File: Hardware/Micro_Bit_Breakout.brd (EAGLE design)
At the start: 68.6 x 12.7 mm, 9 parts, among them J1 M22LOCK, X1 EDGE-80PTH-RA

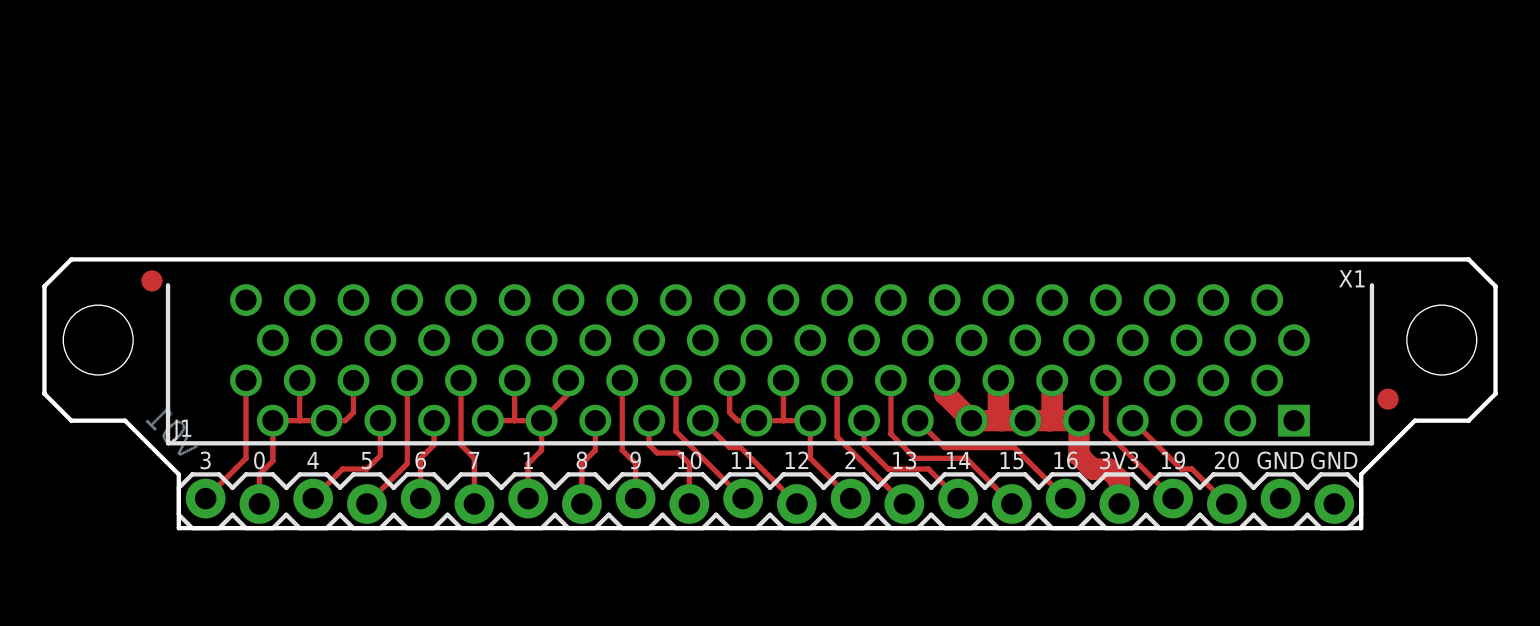
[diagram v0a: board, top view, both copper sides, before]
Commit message: Moved brd outline down
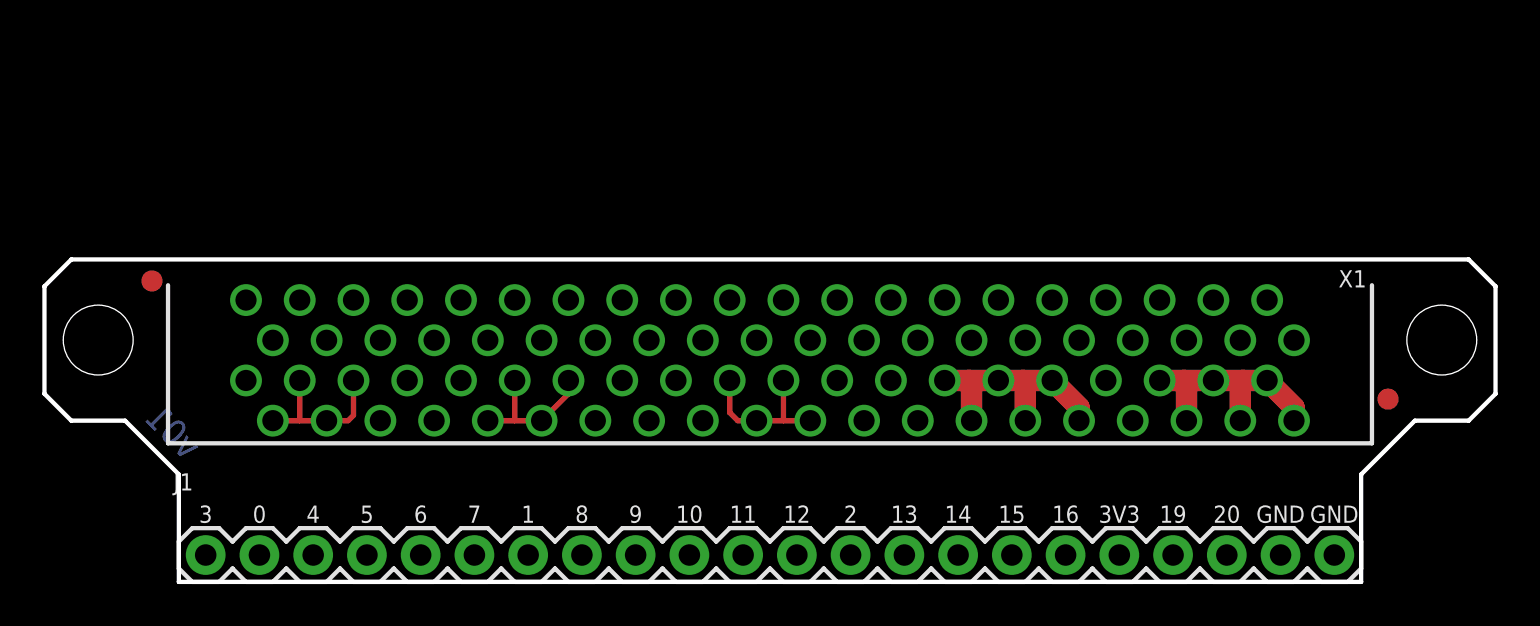
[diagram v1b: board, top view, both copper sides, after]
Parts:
- J1: value M22LOCK -> M22PTH; device SparkFun-Connectors:1X22_LOCK -> local_lib:1X22
- X1: device SparkFun-Connectors:VEC-127-080-R -> local_lib:VEC-127-080-R
- moved J1 2.54 mm to (61.0, -1.27)
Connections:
- net N$10 renamed 12
- net N$11 renamed 11
- net N$12 renamed 10
- net N$13 renamed 9
- net N$14 renamed 8
- net N$15 renamed 1
- net N$17 renamed 7
- net N$18 renamed 6
- net N$19 renamed 5
- net N$2 renamed 16
- net N$20 renamed 4
- net N$21 renamed 0
- net N$22 renamed 3
- net N$3 renamed 20
- net N$4 renamed 19
- net N$5 renamed 3V3
- net N$6 renamed 15
- net N$7 renamed 14
- net N$8 renamed 13
- net N$9 renamed 2
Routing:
- net GND: track 0.00 -> 11.4 mm
- net 15: track 9.62 -> 0.00 mm
- net 16: track 8.51 -> 0.00 mm
- net 13: track 7.15 -> 0.00 mm
- net 19: track 6.90 -> 0.00 mm
- net 11: track 6.90 -> 0.00 mm
- net 14: track 6.64 -> 0.00 mm
- net 5: track 6.63 -> 0.00 mm
- net 3: track 6.37 -> 0.00 mm
- net 7: track 6.10 -> 0.00 mm
- net 12: track 6.08 -> 0.00 mm
- net 20: track 6.08 -> 0.00 mm
- net 9: track 5.85 -> 0.00 mm
- net 4: track 5.67 -> 0.00 mm
- net 10: track 5.32 -> 0.00 mm
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- removed copper zone on layer 1, net GND
- removed copper zone on layer 16, net GND
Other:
- board size 68.6 x 12.7 mm -> 68.6 x 15.2 mm

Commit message: Changed layout to have pin numbers in order. Added prettier silk.
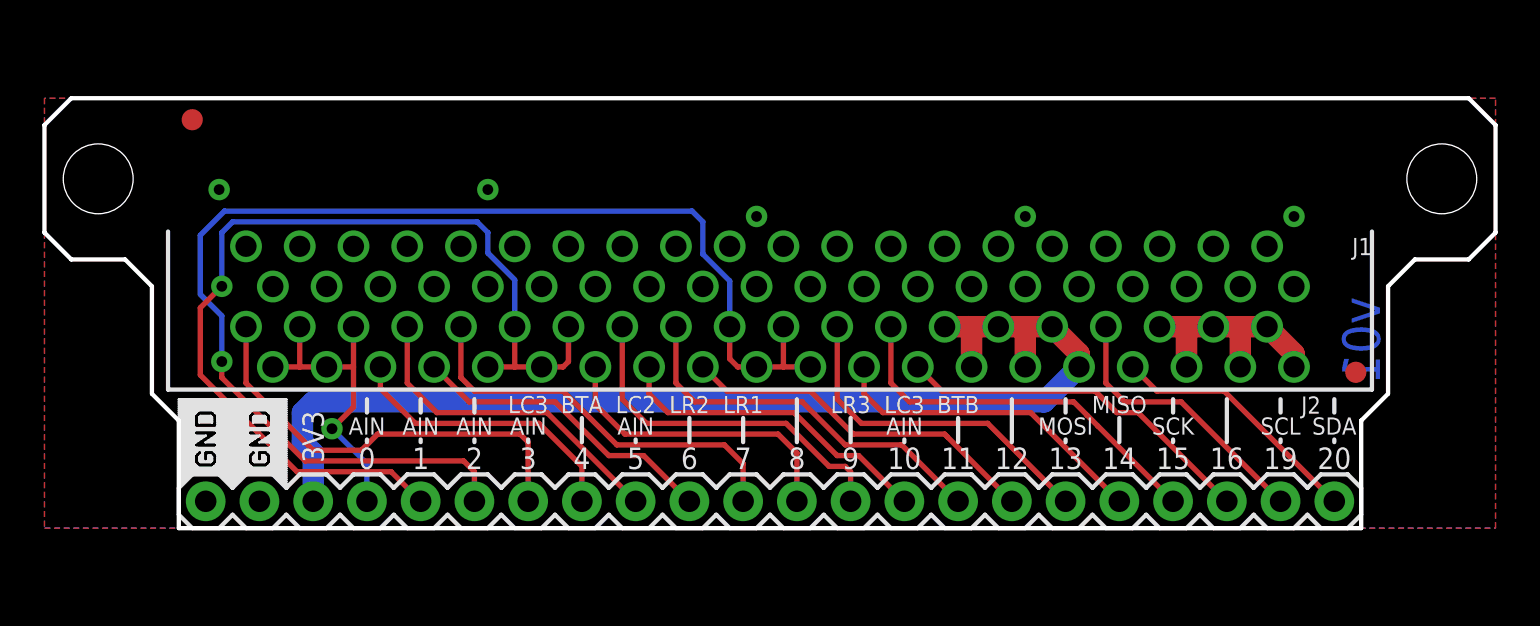
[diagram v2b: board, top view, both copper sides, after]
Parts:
- removed LOGO1: SFE_LOGO_FLAME.1_INCH, SparkFun-Aesthetics:SFE_LOGO_FLAME_.1
- removed X1: EDGE-80PTH-RA, local_lib:VEC-127-080-R
- added J2: M22PTH, local_lib:1X22
- added LOGO2: SFE_LOGO_NAME_FLAME.1_INCH, SparkFun-Aesthetics:SFE_LOGO_NAME_FLAME_.1
- added U$1, U$2: (no value), negasilk:NEGASILK_MICRO_BIT_BREAKOUT
- J1: value M22PTH -> EDGE-80PTH-RA; device local_lib:1X22 -> local_lib:VEC-127-080-R
- moved LOGO3 50.2 mm to (12.4, 17.1)
- moved J1 28.1 mm to (34.3, 7.62)
- moved FRAME1 12.0 mm to (0.00, -11.4)
- moved FD1 7.85 mm to (6.99, 19.3)
- moved H1 7.62 mm to (2.54, 16.5)
- moved H2 7.62 mm to (66.0, 16.5)
- moved FD2 1.98 mm to (62.0, 7.37)
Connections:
- net 0: now also J1.A36, J1.A37, J1.A38, J1.A39, J2.4; no longer J1.21, X1.A36, X1.A37, X1.A38, X1.A39
- net 1: now also J1.A28, J1.A29, J1.A30, J1.A31, J2.5; no longer J1.16, X1.A28, X1.A29, X1.A30, X1.A31
- net 10: now also J1.A25, J2.14; no longer J1.13, X1.A25
- net 11: now also J1.A24, J2.15; no longer J1.12, X1.A24
- net 12: now also J1.A23, J2.16; no longer J1.11, X1.A23
- net 13: now also J1.A18, J2.17; no longer J1.9, X1.A18
- net 14: now also J1.A17, J2.18; no longer J1.8, X1.A17
- net 15: now also J1.A16, J2.19; no longer J1.7, X1.A16
- net 16: now also J1.A15, J2.20; no longer J1.6, X1.A15
- net 19: now also J1.A8, J2.21; no longer J1.4, X1.A8
- net 2: now also J1.A19, J1.A20, J1.A21, J1.A22, J2.6; no longer J1.10, X1.A19, X1.A20, X1.A21, X1.A22
- net 20: now also J1.A7, J2.22; no longer J1.3, X1.A7
- net 3: now also J1.A40, J2.7; no longer J1.22, X1.A40
- net 3V3: now also J1.A10, J1.A11, J1.A12, J1.A13, J1.A14, J1.A9, J2.3; no longer J1.5, X1.A10, X1.A11, X1.A12, X1.A13, X1.A14, X1.A9
- net 4: now also J1.A35, J2.8; no longer J1.20, X1.A35
- net 5: now also J1.A34, J2.9; no longer J1.19, X1.A34
- net 6: now also J1.A33, J2.10; no longer J1.18, X1.A33
- net 7: now also J1.A32, J2.11; no longer J1.17, X1.A32
- net 8: now also J1.A27, J2.12; no longer J1.15, X1.A27
- net 9: now also J1.A26, J2.13; no longer J1.14, X1.A26
- net GND: now also J1.A1, J1.A2, J1.A3, J1.A4, J1.A5, J1.A6, J2.1, J2.2; no longer J1.1, J1.2, X1.A1, X1.A2, X1.A3, X1.A4, X1.A5, X1.A6
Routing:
- net 2: track 7.39 -> 59.6 mm, vias 0 -> 1
- net 3V3: track 11.4 -> 53.4 mm
- net 1: track 6.87 -> 45.5 mm, vias 0 -> 1
- net 3: track 0.00 -> 20.6 mm
- net 7: track 0.00 -> 19.2 mm
- net 15: track 0.00 -> 18.3 mm
- net 11: track 0.00 -> 18.3 mm
- net 12: track 0.00 -> 17.2 mm
- net 16: track 0.00 -> 17.2 mm
- net 9: track 0.00 -> 17.0 mm
- net 13: track 0.00 -> 16.2 mm
- net 5: track 0.00 -> 15.8 mm
- net 10: track 0.00 -> 15.4 mm
- net 14: track 0.00 -> 15.4 mm
- net 6: track 0.00 -> 14.7 mm
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- added copper zone on layer 1, net GND
- added copper zone on layer 16, net GND
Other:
- board size 68.6 x 15.2 mm -> 68.6 x 20.3 mm
- board text added: "AIN"
- board text added: "BTA"
- board text added: "BTB"
- board text added: "LC2"
- board text added: "LC3"
- board text added: "LR1"
- board text added: "LR2"
- board text added: "LR3"
- board text added: "MISO"
- board text added: "MOSI"
- board text added: "SCK"
- board text added: "SCL"
- board text added: "SDA"
- board text removed: "GND"

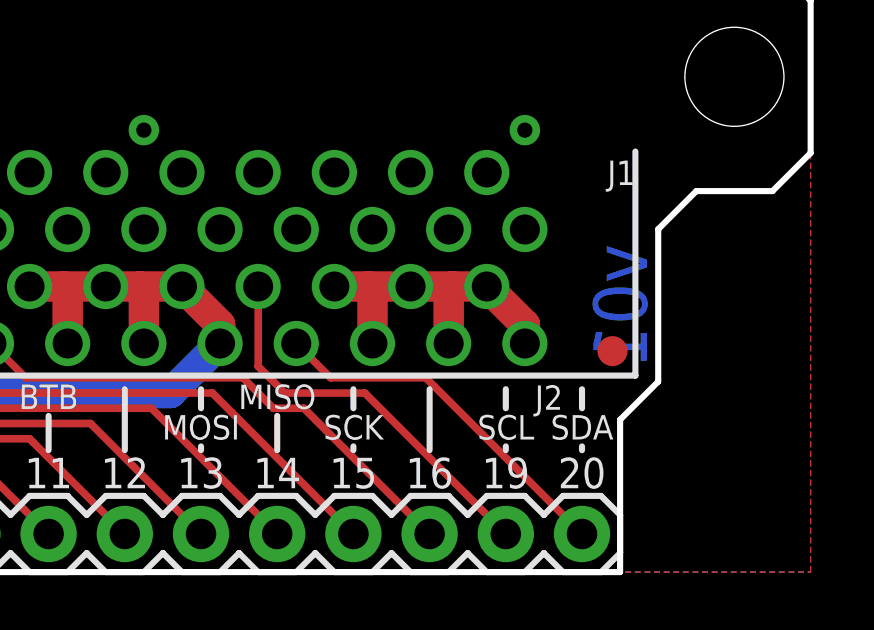
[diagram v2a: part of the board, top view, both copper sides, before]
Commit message: Added dimension for origin to end of edge connector. Added pin 1 dot in silk for edge connector.
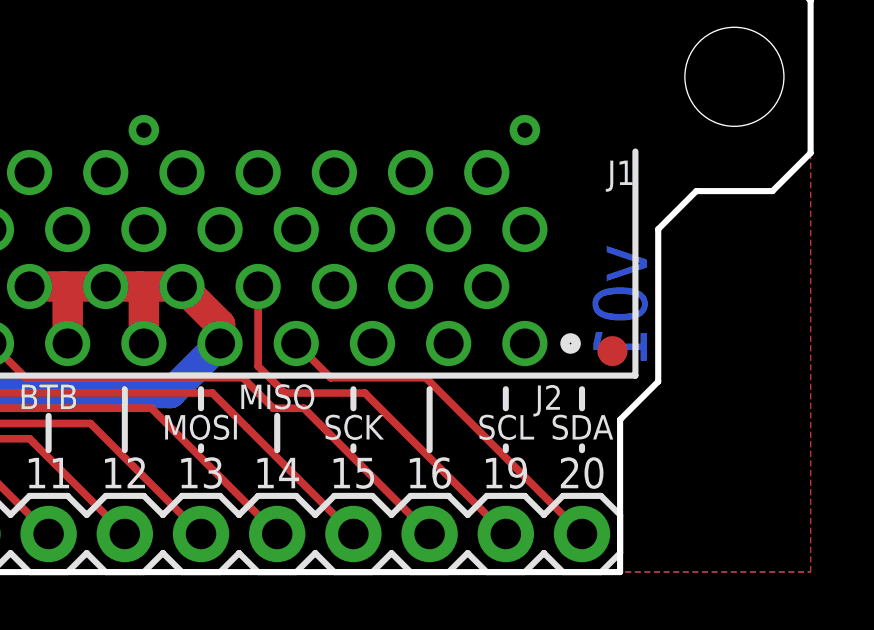
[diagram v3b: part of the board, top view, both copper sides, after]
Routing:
- net GND: track 11.4 -> 0.00 mm
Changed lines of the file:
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@@
 <dimension x1="64.8716" y1="15.3416" x2="67.2084" y2="17.6784" x3="69.5198" y3="13.030196875" textsize="1.778" textratio="15" layer="47" unit="inch"/>
 <dimension x1="0" y1="0" x2="0" y2="16.51" x3="-13.97" y3="8.255" textsize="1.778" textratio="15" layer="47" unit="inch"/>
-<dimension x1="2.54" y1="16.51" x2="0" y2="16.51" x3="1.27" y3="26.67" textsize="1.778" textratio="15" layer="47" unit="inch"/>
+<dimension x1="2.54" y1="16.51" x2="0" y2="16.51" x3="1.27" y3="29.21" textsize="1.778" textratio="15" layer="47" unit="inch"/>
+<dimension x1="0" y1="0" x2="5.842" y2="27.94" x3="-35.56" y3="13.97" textsize="1.778" textratio="15" layer="47" dtype="vertical" unit="inch"/>
 </plain>
 <attributes>
@@
 <contactref element="J2" pad="2"/>
 <contactref element="J2" pad="1"/>
-<wire x1="59.055" y1="7.62" x2="59.055" y2="8.25" width="1.016" layer="1"/>
-<wire x1="59.055" y1="8.25" x2="57.785" y2="9.52" width="1.016" layer="1"/>
-<wire x1="57.785" y1="9.52" x2="56.642" y2="9.52" width="1.016" layer="1"/>
-<wire x1="56.642" y1="9.52" x2="55.245" y2="9.52" width="1.016" layer="1"/>
-<wire x1="55.245" y1="9.52" x2="53.848" y2="9.52" width="1.016" layer="1"/>
-<wire x1="53.848" y1="9.52" x2="52.705" y2="9.52" width="1.016" layer="1"/>
-<wire x1="53.975" y1="7.62" x2="53.975" y2="9.393" width="1.016" layer="1"/>
-<wire x1="53.975" y1="9.393" x2="53.848" y2="9.52" width="1.016" layer="1"/>
-<wire x1="56.515" y1="7.62" x2="56.515" y2="9.393" width="1.016" layer="1"/>
-<wire x1="56.515" y1="9.393" x2="56.642" y2="9.52" width="1.016" layer="1"/>
 <polygon width="0.254" layer="1" isolate="0.3048">
 <vertex x="0" y="20.32"/>

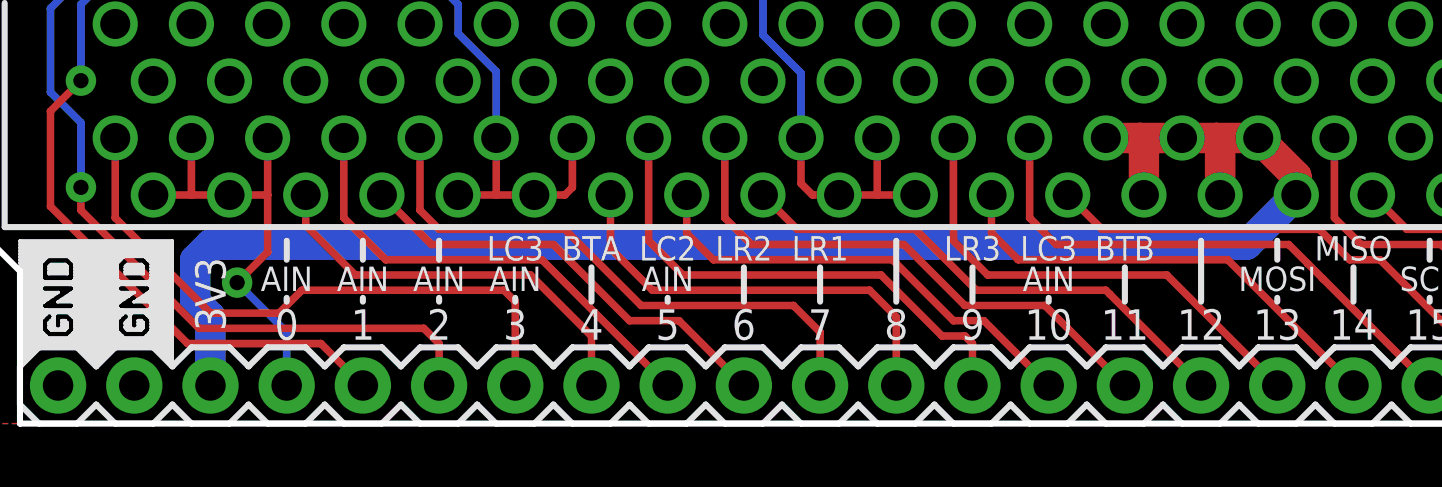
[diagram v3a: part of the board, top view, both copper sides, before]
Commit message: Changed 3V3 net to 3.3V symbol
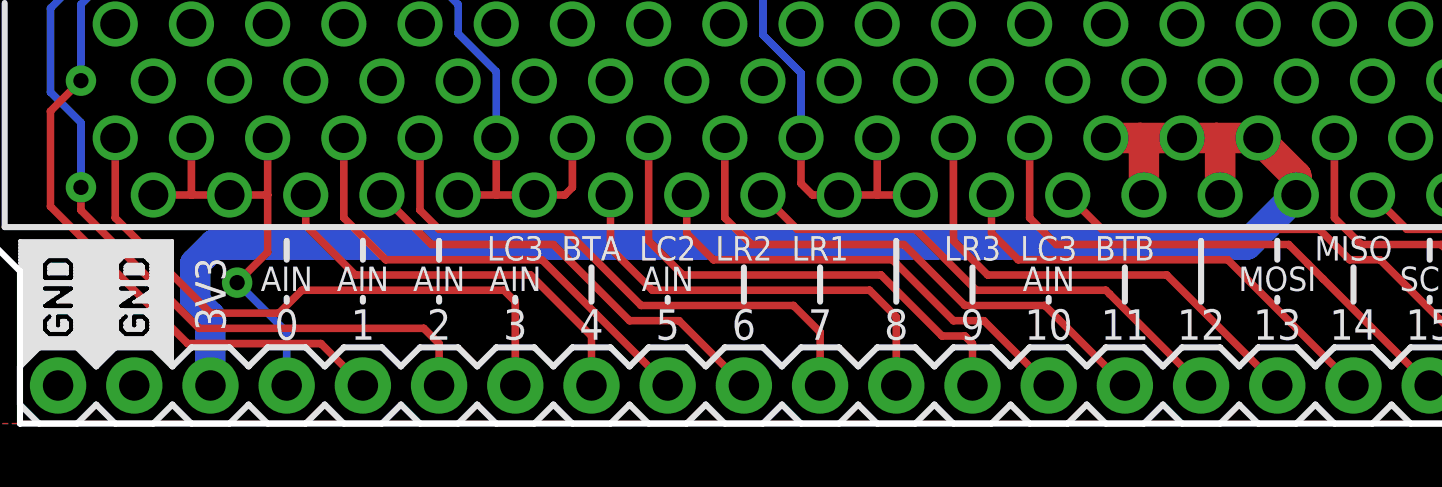
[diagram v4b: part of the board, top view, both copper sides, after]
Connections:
- net 3V3 renamed 3.3V
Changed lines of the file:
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@@
 <setting verticaltext="up"/>
 </settings>
-<grid distance="0.05" unitdist="inch" unit="inch" style="dots" multiple="1" display="yes" altdistance="0.025" altunitdist="inch" altunit="inch"/>
+<grid distance="0.01" unitdist="inch" unit="inch" style="dots" multiple="1" display="yes" altdistance="0.005" altunitdist="inch" altunit="inch"/>
 <layers>
 <layer number="1" name="Top" color="4" fill="1" visible="yes" active="yes"/>
@@
 <wire x1="53.721" y1="5.969" x2="58.42" y2="1.27" width="0.254" layer="1"/>
 </signal>
-<signal name="3V3">
-<contactref element="J1" pad="A9"/>
-<contactref element="J1" pad="A10"/>
-<contactref element="J1" pad="A11"/>
-<contactref element="J1" pad="A12"/>
-<contactref element="J1" pad="A13"/>
-<contactref element="J1" pad="A14"/>
-<wire x1="48.895" y1="7.62" x2="48.895" y2="8.25" width="1.016" layer="1"/>
-<wire x1="48.895" y1="8.25" x2="47.625" y2="9.52" width="1.016" layer="1"/>
-<wire x1="47.625" y1="9.52" x2="46.228" y2="9.52" width="1.016" layer="1"/>
-<wire x1="46.228" y1="9.52" x2="45.085" y2="9.52" width="1.016" layer="1"/>
-<wire x1="45.085" y1="9.52" x2="43.688" y2="9.52" width="1.016" layer="1"/>
-<wire x1="43.688" y1="9.52" x2="42.545" y2="9.52" width="1.016" layer="1"/>
-<wire x1="46.355" y1="7.62" x2="46.355" y2="9.393" width="1.016" layer="1"/>
-<wire x1="46.355" y1="9.393" x2="46.228" y2="9.52" width="1.016" layer="1"/>
-<wire x1="43.815" y1="7.62" x2="43.815" y2="9.393" width="1.016" layer="1"/>
-<wire x1="43.815" y1="9.393" x2="43.688" y2="9.52" width="1.016" layer="1"/>
-<contactref element="J2" pad="3"/>
-<wire x1="12.7" y1="5.969" x2="47.244" y2="5.969" width="1.016" layer="16"/>
-<wire x1="47.244" y1="5.969" x2="48.895" y2="7.62" width="1.016" layer="16"/>
-<wire x1="12.7" y1="5.969" x2="12.192" y2="5.461" width="1.016" layer="16"/>
-<wire x1="12.192" y1="5.461" x2="12.192" y2="4.064" width="1.016" layer="16"/>
-<wire x1="12.192" y1="4.064" x2="12.7" y2="3.556" width="1.016" layer="16"/>
-<wire x1="12.7" y1="3.556" x2="12.7" y2="1.27" width="1.016" layer="16"/>
-</signal>
 <signal name="16">
 <contactref element="J1" pad="A15"/>
@@
 <via x="20.955" y="16.002" extent="1-16" drill="0.508"/>
 </signal>
+<signal name="3.3V">
+<contactref element="J1" pad="A14"/>
+<contactref element="J1" pad="A9"/>
+<contactref element="J1" pad="A10"/>
+<contactref element="J1" pad="A13"/>
+<contactref element="J1" pad="A12"/>
+<contactref element="J1" pad="A11"/>
+<contactref element="J2" pad="3"/>
+<wire x1="12.7" y1="1.27" x2="12.7" y2="3.556" width="1.016" layer="16"/>
+<wire x1="12.7" y1="3.556" x2="12.192" y2="4.064" width="1.016" layer="16"/>
+<wire x1="12.192" y1="4.064" x2="12.192" y2="5.334" width="1.016" layer="16"/>
+<wire x1="12.192" y1="5.334" x2="12.827" y2="5.969" width="1.016" layer="16"/>
+<wire x1="12.827" y1="5.969" x2="47.244" y2="5.969" width="1.016" layer="16"/>
+<wire x1="48.895" y1="7.62" x2="48.895" y2="8.25" width="1.016" layer="1"/>
+<wire x1="48.895" y1="8.25" x2="47.625" y2="9.52" width="1.016" layer="1"/>
+<wire x1="47.625" y1="9.52" x2="46.228" y2="9.52" width="1.016" layer="1"/>
+<wire x1="46.228" y1="9.52" x2="45.085" y2="9.52" width="1.016" layer="1"/>
+<wire x1="45.085" y1="9.52" x2="43.688" y2="9.52" width="1.016" layer="1"/>
+<wire x1="43.688" y1="9.52" x2="42.545" y2="9.52" width="1.016" layer="1"/>
+<wire x1="43.815" y1="7.62" x2="43.815" y2="9.393" width="1.016" layer="1"/>
+<wire x1="43.815" y1="9.393" x2="43.688" y2="9.52" width="1.016" layer="1"/>
+<wire x1="46.355" y1="7.62" x2="46.355" y2="9.393" width="1.016" layer="1"/>
+<wire x1="46.355" y1="9.393" x2="46.228" y2="9.52" width="1.016" layer="1"/>
+<wire x1="47.244" y1="5.969" x2="48.895" y2="7.62" width="1.016" layer="16"/>
+</signal>
 </signals>
